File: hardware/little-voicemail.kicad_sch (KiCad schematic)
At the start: 17 parts, among them J1 RPi 40-pin (stacking), J2 Contact 1, J3 Contact 2, J4 Contact 3, J5 Contact 4, J6 Contact 5, J7 Contact 6, J8 Push to talk, U1 MCP23017

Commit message: Redesign audio HW: custom HAT with MAX98357A amp + I2S mics
The ReSpeaker HAT's onboard amp is hard-capped at 1 W and was already
maxed out in software (tools/set-audio-levels.sh, the ringtone/mic-gain
commits) - the BOM's 3 W speaker was being starved to a third of its
rating. Fixing that needs a bigger amp, which means a custom board.

Replaces the ReSpeaker 2-Mics HAT with a single custom HAT carrying:
- MAX98357A: I2S-in Class-D amp, 3.2 W into 4 Ohm @ 5V - drives the
  speaker at close to its actual rating instead of a third of it.
- 2x ICS-43434 I2S MEMS mic breakouts (Adafruit #6049), TDM-shared on
  one capture line - factory-trimmed, no mic-bias network or capture
  gain tuning needed.
- The existing MCP23017 button/lamp circuit, unchanged.

Chose the pre-built mic breakout over a bare LGA part on this board:
silicon-vendor datasheet hosts (Analog Devices, TI, Mouser) were
unreachable from this session's network egress, so the MAX98357A's
pinout is cross-checked against an independently published KiCad
symbol rather than typed from memory - I could not do the same for
the ICS-43434's exact LGA pad numbering, so it's specified as a
verified module rather than a footprint I'd be guessing at.

HARDWARE.md: full rewrite of the audio sections and BOM, with real
distributor links (RS, Digi-Key, Mouser, The Pi Hut) for every new
part. Kept the button/lamp GPIO-budget reasoning, which didn't change.

hardware/little-voicemail.kicad_sch: added U2 (MAX98357A), J9/J10
(mic breakout headers), J11 (speaker), C2/C3 (amp decoupling), and
the I2S wiring to the Pi header. While adding that I found the
header's GPIO18/19/20/21 pins wired to stray power-rail flags instead
of signal labels and fixed those. I did *not* touch two similar-looking
issues near the existing SDA/SCL wiring and J1 pin 1 that I couldn't
fully verify without KiCad's ERC - flagged in hardware/README.md.

No .kicad_pcb: this session had no KiCad/kicad-cli to place footprints,
route, or run DRC, so hardwar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
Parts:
- added C2: 100n, Capacitor_SMD:C_0603_1608Metric, symbol LV:C
- added C3: 10u, Capacitor_SMD:C_0805_2012Metric, symbol LV:C
- added J10: Mic right, Connector_PinSocket_2.54mm:PinSocket_1x06_P2.54mm_Vertical, symbol LV:Mic_Conn_6
- added J11: Speaker, Connector_JST:JST_PH_S2B-PH-K_1x02_P2.00mm_Vertical, symbol LV:Speaker_Conn_2
- added J9: Mic left, Connector_PinSocket_2.54mm:PinSocket_1x06_P2.54mm_Vertical, symbol LV:Mic_Conn_6
- added U2: MAX98357A, Package_DFN_QFN:QFN-16-1EP_3x3mm_P0.5mm_EP1.65x1.65mm, symbol LV:MAX98357A
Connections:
- net +3V3: now also J10.1 (VDD), J10.6 (SEL), J9.6 (SEL)
- net +5V: now also C2.2, C3.2, U2.11 (GND), U2.15 (GND); no longer J1.2 (5V), J1.4 (5V)
- net GND: now also C2.1, C3.1, J10.5 (SD), J9.1 (VDD), J9.5 (SD), U2.7 (VDD), U2.8 (VDD); no longer J1.30 (GND)
- net SCL: no longer J1.5 (GPIO3_SCL)
- new net BCLK: J1.30 (GND), J10.4 (WS), J9.4 (WS)
- new net I2S_DIN: J1.4 (5V), J10.2 (GND), J9.2 (GND)
- new net I2S_DOUT: J1.2 (5V)
- new net LRCLK: J1.5 (GPIO3_SCL), J10.3 (SCK), J9.3 (SCK)
- new net SPK+: J11.2 (SPK-)
- new net SPK-: J11.1 (SPK+), U2.10 (OUTN)
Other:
- note added: "AUDIO BLOCK. Pin table and net list cross-checked against https://github.com/IMMRMKW/KICAD (MAX98357A) - see HARDWARE.md and hardware/README.md for the ICS-43434 breakout-vs-bare-die reasoning and for what still needs doing in KiCad before fab (footprint placement and copper routing were not done here)."
- note added: "GPIO18/19/20/21 (I2S) now carry BCLK/LRCLK/I2S_DIN/I2S_DOUT to the audio block at right - this board no longer stacks under a ReSpeaker HAT. SPI0 (7-11) is still free if you want it for something else."
- note removed: "Unused header pins are left open on purpose: this board stacks under the ReSpeaker HAT, which uses I2S (18-21), I2C (2-3) and SPI (7-11)."
- title: Little Voicemail - button and lamp board -> Little Voicemail - audio + button/lamp HAT

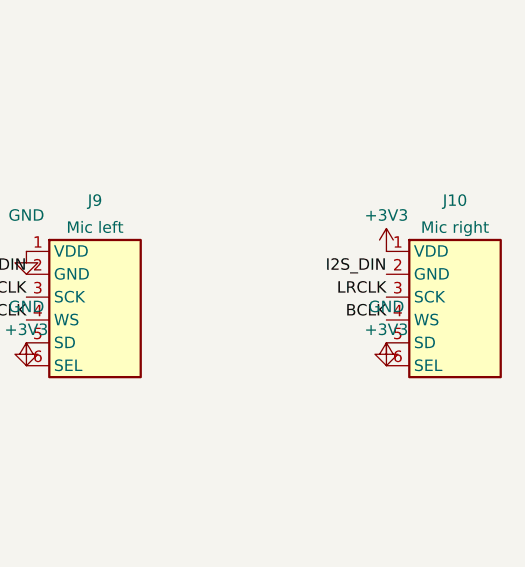
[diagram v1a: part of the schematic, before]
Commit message: Drop to a single mic (J10) per request
J9 already had SEL tied to GND (left slot), so it needs no change -
just remove J10 and its power/ground/clock labels.

Co-Authored-By: Claude Sonnet 5 <noreply@anthropic.com>
Claude-Session: https://claude.ai/code/session_01E78hZPbGcYZMEw3nS4sMbw
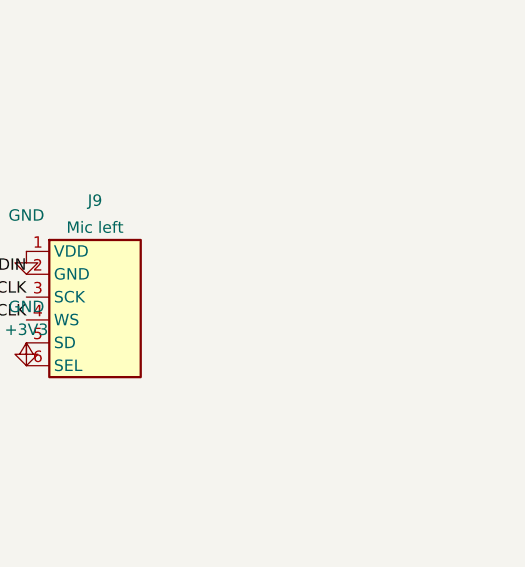
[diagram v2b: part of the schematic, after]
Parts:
- removed J10: Mic right, Connector_PinSocket_2.54mm:PinSocket_1x06_P2.54mm_Vertical, symbol LV:Mic_Conn_6
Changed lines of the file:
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@@
     (instances (project "little-voicemail"
       (path "/3a3426fd-a5c2-45f5-a94e-3d2e6520e0af" (reference "#PWR0053") (unit 1)))))
-  (symbol (lib_id "LV:Mic_Conn_6") (at 560.0 130.0 0) (unit 1)
-    (in_bom yes) (on_board yes) (dnp no)
-    (property "Reference" "J10" (at 560.0 118.0 0) (effects (font (size 1.27 1.27))))
-    (property "Value" "Mic right" (at 560.0 121.0 0) (effects (font (size 1.27 1.27))))
-    (property "Footprint" "Connector_PinSocket_2.54mm:PinSocket_1x06_P2.54mm_Vertical" (at 560.0 130.0 0) (effects (font (size 1.27 1.27)) hide))
-    (pin "1")
-    (pin "2")
-    (pin "3")
-    (pin "4")
-    (pin "5")
-    (pin "6")
-    (instances (project "little-voicemail"
-      (path "/3a3426fd-a5c2-45f5-a94e-3d2e6520e0af" (reference "J10") (unit 1)))))
-  (symbol (lib_id "power:+3V3") (at 552.38 136.35 0) (unit 1)
-    (in_bom no) (on_board yes) (dnp no)
-    (property "Reference" "#PWR0054" (at 552.38 140.35 0) (effects (font (size 1.27 1.27)) hide))
-    (property "Value" "+3V3" (at 552.38 132.35 0) (effects (font (size 1.27 1.27))))
-    (pin "1")
-    (instances (project "little-voicemail"
-      (path "/3a3426fd-a5c2-45f5-a94e-3d2e6520e0af" (reference "#PWR0054") (unit 1)))))
-  (symbol (lib_id "power:GND") (at 552.38 133.81 0) (unit 1)
-    (in_bom no) (on_board yes) (dnp no)
-    (property "Reference" "#PWR0055" (at 552.38 137.81 0) (effects (font (size 1.27 1.27)) hide))
-    (property "Value" "GND" (at 552.38 129.81 0) (effects (font (size 1.27 1.27))))
-    (pin "1")
-    (instances (project "little-voicemail"
-      (path "/3a3426fd-a5c2-45f5-a94e-3d2e6520e0af" (reference "#PWR0055") (unit 1)))))
-  (label "BCLK" (at 552.38 131.27 0)
-    (effects (font (size 1.27 1.27)) (justify right bottom)))
-  (label "LRCLK" (at 552.38 128.73 0)
-    (effects (font (size 1.27 1.27)) (justify right bottom)))
-  (label "I2S_DIN" (at 552.38 126.19 0)
-    (effects (font (size 1.27 1.27)) (justify right bottom)))
-  (symbol (lib_id "power:+3V3") (at 552.38 123.65 0) (unit 1)
-    (in_bom no) (on_board yes) (dnp no)
-    (property "Reference" "#PWR0056" (at 552.38 127.65 0) (effects (font (size 1.27 1.27)) hide))
-    (property "Value" "+3V3" (at 552.38 119.65 0) (effects (font (size 1.27 1.27))))
-    (pin "1")
-    (instances (project "little-voicemail"
-      (path "/3a3426fd-a5c2-45f5-a94e-3d2e6520e0af" (reference "#PWR0056") (unit 1)))))
   (sheet_instances
     (path "/" (page "1")))

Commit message: Swap speaker for a JST-connectorized enclosed one; fix J11 footprint
Speaker: Adafruit Mono Enclosed Speaker (3W 4ohm, #3351) via The Pi
Hut, ~£3.40, with a pre-attached 150mm JST-PH 2-pin cable - no
soldering to the speaker. Drops the RS PRO part, whose price I'd
misquoted earlier (~£3 stated, actually £7.29 single-unit) and which
only had bare leads anyway.

J11 footprint was wrong: JST names its vertical and right-angle PH
variants with different prefixes (B2B = vertical, S2B = right-angle),
and the schematic had them crossed - "S2B-PH-K" paired with
"_Vertical". Fixed to B2B-PH-K-S (vertical, ~$0.12, Mouser/Digikey),
which is also the correct mate for the new speaker's cable.

Also cleans up leftover two-mic (J10) references in both docs that
the prior single-mic schematic edit missed - BOM quantities, netlist,
pinout tables, and a couple of "no respin needed" claims that were
overstated given J10 no longer exists on the schematic at all.

Co-Authored-By: Claude Sonnet 5 <noreply@anthropic.com>
Claude-Session: https://claude.ai/code/session_01E78hZPbGcYZMEw3nS4sMbw
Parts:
- J11: footprint Connector_JST:JST_PH_S2B-PH-K_1x02_P2.00mm_Vertical -> Connector_JST:JST_PH_B2B-PH-K_1x02_P2.00mm_Vertical
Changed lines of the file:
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@@
   (title_block
     (title "Little Voicemail - audio + button/lamp HAT")
-    (date "2026-09-11")
-    (rev "B")
+    (date "2026-09-30")
+    (rev "C")
     (comment 1 "Six contact buttons + push-to-talk on one MCP23017 at 0x20")
-    (comment 2 "MAX98357A (I2S amp) drives the speaker; 2x ICS-43434 breakouts")
-    (comment 3 "give far-field mic input, TDM-shared on one I2S capture line")
+    (comment 2 "MAX98357A (I2S amp) drives the speaker via J11 (JST-PH B2B-PH-K-S)")
+    (comment 3 "ICS-43434 breakout (J9) gives far-field mic input over I2S")
     (comment 4 "Lamps are ACTIVE LOW: anode to +5V via R, cathode to GPBn")
   )
@@
     (property "Reference" "J11" (at 520.0 82.0 0) (effects (font (size 1.27 1.27))))
     (property "Value" "Speaker" (at 520.0 85.0 0) (effects (font (size 1.27 1.27))))
-    (property "Footprint" "Connector_JST:JST_PH_S2B-PH-K_1x02_P2.00mm_Vertical" (at 520.0 90.0 0) (effects (font (size 1.27 1.27)) hide))
-    (pin "1")
-    (pin "2")
+    (property "Footprint" "Connector_JST:JST_PH_B2B-PH-K_1x02_P2.00mm_Vertical" (at 520.0 90.0 0) (effects (font (size 1.27 1.27)) hide))
+    (pin "1")
+    (pin "2")
